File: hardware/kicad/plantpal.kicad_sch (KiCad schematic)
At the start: 58 parts, among them Q1 DMG1012UW, Q2 AO3407, Q3 PMV32UP, Q4 DMG1012UW, Q5 PMV32UP, SW3 RESET, SW4 BOOT, U2 AEM10941-QFN, U3 XC6220, U4 BME688, U5 TPL5110DDCR, U7 ESP32-C6FH4

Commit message: add ext crystal and rtc crystal
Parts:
- added C22, C23: ~, symbol Device:C_Small
- added C3, C4: 12p, symbol Device:C_Small
- added R14, R15: ~, symbol Device:R_Small
- added Y1: CM315D32768DZFT, symbol Device:Crystal_Small
- added Y2: R940000171, symbol Device:Crystal_Small
- renumbered C11 to C1, C17 to C10, C5 to C11, C7 to C12, C8 to C13, C18 to C14, C10 to C15, C19 to C16, C14 to C17, C15 to C18, C12 to C19, C9 to C2, C13 to C20, C6 to C21, C4 to C5, C3 to C6, C2 to C7, C16 to C8, C1 to C9, L2 to L1, L1 to L2, Q2 to Q1, Q3 to Q2, Q4 to Q3, Q1 to Q4, R10 to R1, R15 to R10, R3 to R11, R5 to R12, R4 to R13, R8 to R2, R17 to R3, R18 to R4, R19 to R5, R20 to R6, R6 to R7, R1 to R8, R16 to R9, SW4 to SW1, SW3 to SW2, TP8 to TP2, TP9 to TP3, TP2 to TP4, TP3 to TP5, TP11 to TP6, U7 to U1, U4 to U2, U2 to U3, U3 to U4
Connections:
- net GND: now also C22.1, C23.1, C3.1, C4.1
- net at U1.30 (XTAL_N): now also C22.2, Y2.2
- net at U1.31 (XTAL_P): now also R14.2
- net at U1.6 (GPIO0/XTAL_32K_P/ADC1_CH0): now also R15.1
- net at U1.7 (GPIO1/XTAL_32K_N/ADC1_CH1): now also C4.2, Y1.1
- new net: C23.2, R14.1, Y2.1
- new net: C3.2, R15.2, Y1.2
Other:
- note added: "TODO: Look for other example of 40MHz Crystal"

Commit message: add esp32, usb, charger, power gate, and soil moisture
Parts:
- added AE1: Antenna_Chip, symbol Device:Antenna_Chip
- added C24, C25: DNP, Capacitor_SMD:C_0603_1608Metric_Pad1.08x0.95mm_HandSolder, symbol Device:C_Small
- added C26: 10n, Capacitor_SMD:C_0402_1005Metric, symbol Device:C
- added C27: 100n, Capacitor_SMD:C_0402_1005Metric, symbol Device:C
- added C28: 10u, Capacitor_SMD:C_0603_1608Metric, symbol Device:C_Small
- added C29: 10u, Capacitor_SMD:C_0805_2012Metric, symbol Device:C_Small
- added C30: 1n, Capacitor_SMD:C_0402_1005Metric, symbol Device:C_Small
- added D1: ORANGE, LED_SMD:LED_0603_1608Metric, symbol Device:LED
- added D2: B5819W, Diode_SMD:D_SOD-123, symbol Diode:MBR0540
- added D3: LL4148, Diode_SMD:D_MiniMELF, symbol Diode:LL4148
- added F1: 0.75A, Fuse:Fuse_0805_2012Metric, symbol Device:Polyfuse
- added FB1: MMZ1608B601CTAH0, Inductor_SMD:L_0603_1608Metric, symbol Penguino-STM32WL-LoRa-E5-rescue:Ferrite_Bead-Device
- added J1: U262-161N-4BVC11, bwlr1e_prog:USB_C_Receptacle_XKB_U262-16XN-4BVC11, symbol Connector:USB_C_Receptacle_USB2.0
- added L4: 0, Inductor_SMD:L_0603_1608Metric_Pad1.05x0.95mm_HandSolder, symbol Device:L_Small
- added Q6: MMBT3906, Package_TO_SOT_SMD:SOT-23, symbol Transistor_BJT:MMBT3906
- added R16: 1M, Resistor_SMD:R_0603_1608Metric_Pad0.98x0.95mm_HandSolder, symbol Device:R_Small
- added R17, R18: 5.1K, Resistor_SMD:R_0402_1005Metric, symbol Device:R_Small
- added R19, R24: 10k, Resistor_SMD:R_0402_1005Metric, symbol Device:R_Small_US
- added R20: 10K, Resistor_SMD:R_0402_1005Metric, symbol Device:R_Small
- added R21: 2K, Resistor_SMD:R_0603_1608Metric, symbol Device:R_Small
- added R22: 1M, Resistor_SMD:R_0402_1005Metric, symbol Device:R_Small_US
- added R23: 1K, Resistor_SMD:R_0603_1608Metric, symbol Device:R_Small
- added U6: USBLC6-2P6, Package_TO_SOT_SMD:SOT-666, symbol Power_Protection:USBLC6-2P6
- added U7: MCP73831T-2ACI/OT, Package_TO_SOT_SMD:SOT-23-5, symbol Battery_Management:MCP73831-2-OT
- C5: renamed from C22; value ~ -> 10p
- C6: renamed from C23; value ~ -> 10p
- R15: renamed from R13; value 16.776K -> 16.9K; footprint Resistor_SMD:R_0603_1608Metric -> Resistor_SMD:R_0402_1005Metric
- R3: renamed from R14; value ~ -> 22
- R4: renamed from R15; value ~ -> 22
- Y2: symbol Device:Crystal_Small -> Device:Crystal_GND24_Small
- renumbered C8 to C10, C9 to C11, C10 to C12, C11 to C13, C12 to C14, C13 to C15, C14 to C16, C15 to C17, C16 to C18, C17 to C19, C18 to C20, C19 to C21, C20 to C22, C21 to C23, C5 to C7, C6 to C8, C7 to C9, R8 to R10, R9 to R11, R10 to R12, R11 to R13, R12 to R14, R3 to R5, R4 to R6, R5 to R7, R6 to R8, R7 to R9
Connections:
- net BATT+: now also Q2.2 (S), R7.1
- net DONE: now also R16.1
- net GND: now also Y2.2, Y2.4, AE1.1 (FEED), C24.1, C25.2, C26.2, C27.2, C28.2, C29.1, C30.2, J1.A1 (GND), J1.A12 (GND), J1.B1 (GND), J1.B12 (GND), Q6.3 (C), R16.2, R17.2, R18.2, R21.2, R22.2, U6.2 (GND), U7.2 (VSS)
- net LIPO+: no longer Q2.2 (S), R7.1
- net M_DRV: now also R20.2
- net PWM: now also R19.1, R24.2
- net SENSE_OUT: now also C30.1, D3.1 (K), R22.1
- net at C5.2, U1.30 (XTAL_N): now also Y2.3; no longer Y2.2
- net ANT: now reaches U1.1 (ANT)
- net ANT: now also C25.1, L4.2
- new net: J1.B5 (CC2), R18.1
- new net: C27.1, F1.1, FB1.2
- new net: C26.1, FB1.1, J1.A4 (VBUS), J1.A9 (VBUS), J1.B4 (VBUS), J1.B9 (VBUS)
- new net: J1.A5 (CC1), R17.1
- new net: Q6.1 (B), R24.1
- new net: R23.1, U7.1 (STAT)
- new net: R21.1, U7.5 (PROG)
- new net: AE1.2 (PCB_Trace), C24.2, L4.1
- new net: D1.1 (K), R23.2
- new net: D2.1 (K), R20.1
- new net +BATT: C29.2, U7.3 (VBAT)
- new net CAP_TRACK: D3.2 (A), Q6.2 (E), R19.2
- new net D+: U6.6 (I/O1)
- new net D-: U6.4 (I/O2)
- new net D_IN+: J1.A6 (D+), J1.B6 (D+), U6.1 (I/O1)
- new net D_IN-: J1.A7 (D-), J1.B7 (D-), U6.3 (I/O2)
- new net VBUS: C28.1, D1.2 (A), D2.2 (A), F1.2, U6.5 (VBUS), U7.4 (VDD)
- no-connect marks 7 -> 10
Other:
- note added: "50 ohm Trace Refer to Picoclick-C3 for layout"
- note added: "Around 30s Timer"
- note added: "Battery Charger"
- note added: "Charge LED"
- note added: "Diode might not be needed"
- note added: "NOTE: Pull-down might not be needed for DONE"
- note added: "Place Close to ESP32-C6"
- note added: "Resistor Prog Charge Rate: 10K = 100mA 5K = 200mA 2K = 500mA 1K = 1000mA"
- note added: "Soil Moisture Sense"
- note added: "TODO: - Schematic for EPD"
- note added: "USB-C and ESD Protection"
- note added: "When USB is plugged in pull M_DRV to 3V3"
- note removed: "30s Timer"
- moved on the sheet: C19, C20, C23, C3, C4, C5, C6, R11, R12, R13, R14, R15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

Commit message: separate schematics
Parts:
- removed AE1: Antenna_Chip, symbol Device:Antenna_Chip
- removed BT1: 3.7v LiPo, Connector_JST:JST_PH_S2B-PH-K_1x02_P2.00mm_Horizontal, symbol Device:Battery_Cell
- removed C1: 100n, symbol Device:C_Small
- removed C10: 0.1uF, Capacitor_SMD:C_0603_1608Metric, symbol Device:C
- removed C11, C16, C18, C9: 100n, Capacitor_SMD:C_0603_1608Metric_Pad1.08x0.95mm_HandSolder, symbol Device:C_Small
- removed C12: 10n, Capacitor_SMD:C_0603_1608Metric_Pad1.08x0.95mm_HandSolder, symbol Device:C_Small
- removed C13, C8: 1u, Capacitor_SMD:C_0603_1608Metric_Pad1.08x0.95mm_HandSolder, symbol Device:C_Small
- removed C14: 150u, Capacitor_SMD:C_1210_3225Metric, symbol Device:C_Small
- removed C15: 22u, Capacitor_SMD:C_0603_1608Metric_Pad1.08x0.95mm_HandSolder, symbol Device:C_Small
- removed C17, C21, C22, C7: 10u, Capacitor_SMD:C_0603_1608Metric_Pad1.08x0.95mm_HandSolder, symbol Device:C_Small
- removed C19, C20: 100nF, Capacitor_SMD:C_0603_1608Metric_Pad1.08x0.95mm_HandSolder, symbol Device:C_Small
- removed C2: 1u, symbol Device:C_Small
- removed C23: 100nF, Capacitor_SMD:C_0603_1608Metric, symbol Device:C_Small
- removed C24, C25: DNP, Capacitor_SMD:C_0603_1608Metric_Pad1.08x0.95mm_HandSolder, symbol Device:C_Small
- removed C26: 10n, Capacitor_SMD:C_0402_1005Metric, symbol Device:C
- removed C27: 100n, Capacitor_SMD:C_0402_1005Metric, symbol Device:C
- removed C28: 10u, Capacitor_SMD:C_0603_1608Metric, symbol Device:C_Small
- removed C29: 10u, Capacitor_SMD:C_0805_2012Metric, symbol Device:C_Small
- removed C3, C4: 12p, symbol Device:C_Small
- removed C30: 1n, Capacitor_SMD:C_0402_1005Metric, symbol Device:C_Small
- removed C5, C6: 10p, symbol Device:C_Small
- removed D1: ORANGE, LED_SMD:LED_0603_1608Metric, symbol Device:LED
- removed D2: B5819W, Diode_SMD:D_SOD-123, symbol Diode:MBR0540
- removed D3: LL4148, Diode_SMD:D_MiniMELF, symbol Diode:LL4148
- removed F1: 0.75A, Fuse:Fuse_0805_2012Metric, symbol Device:Polyfuse
- removed FB1: MMZ1608B601CTAH0, Inductor_SMD:L_0603_1608Metric, symbol Penguino-STM32WL-LoRa-E5-rescue:Ferrite_Bead-Device
- removed J1: U262-161N-4BVC11, bwlr1e_prog:USB_C_Receptacle_XKB_U262-16XN-4BVC11, symbol Connector:USB_C_Receptacle_USB2.0
- removed L1: 2n, Inductor_SMD:L_0603_1608Metric_Pad1.05x0.95mm_HandSolder, symbol Device:L_Small
- removed L2: 10u 0.55A, Teapot:IND_LPS4012-103MRB, symbol Device:L_Small
- removed L3: 10u, Inductor_SMD:L_0603_1608Metric_Pad1.05x0.95mm_HandSolder, symbol Device:L_Small
- removed L4: 0, Inductor_SMD:L_0603_1608Metric_Pad1.05x0.95mm_HandSolder, symbol Device:L_Small
- removed Q1: AO3407, Package_TO_SOT_SMD:SOT-23, symbol Device:Q_PMOS_GSD
- removed Q2: PMV32UP, Package_TO_SOT_SMD:SOT-23, symbol Device:Q_PMOS_GSD
- removed Q3, Q4: DMG1012UW, Package_TO_SOT_SMD:SOT-323_SC-70, symbol Device:Q_NMOS_GSD
- removed Q5: PMV32UP, Package_TO_SOT_SMD:SOT-23, symbol Simulation_SPICE:PMOS
- removed Q6: MMBT3906, Package_TO_SOT_SMD:SOT-23, symbol Transistor_BJT:MMBT3906
- removed R1: 5.1K, symbol Device:R_Small
- removed R10, R16: 1M, Resistor_SMD:R_0603_1608Metric_Pad0.98x0.95mm_HandSolder, symbol Device:R_Small
- removed R11, R12: 10K, Resistor_SMD:R_0603_1608Metric_Pad0.98x0.95mm_HandSolder, symbol Device:R_Small
- removed R13, R14, R6: 10K, Resistor_SMD:R_0603_1608Metric, symbol Device:R_Small
- removed R15: 16.9K, Resistor_SMD:R_0402_1005Metric, symbol Device:R_Small
- removed R17, R18: 5.1K, Resistor_SMD:R_0402_1005Metric, symbol Device:R_Small
- removed R19, R24: 10k, Resistor_SMD:R_0402_1005Metric, symbol Device:R_Small_US
- removed R2, R9: 10K, symbol Device:R_Small
- removed R20: 10K, Resistor_SMD:R_0402_1005Metric, symbol Device:R_Small
- removed R21: 2K, Resistor_SMD:R_0603_1608Metric, symbol Device:R_Small
- removed R22: 1M, Resistor_SMD:R_0402_1005Metric, symbol Device:R_Small_US
- removed R23: 1K, Resistor_SMD:R_0603_1608Metric, symbol Device:R_Small
- removed R3, R4: 22, symbol Device:R_Small
- removed R5: 4.7K, Resistor_SMD:R_0603_1608Metric, symbol Device:R_Small
- removed R7, R8: 1M, Resistor_SMD:R_0603_1608Metric, symbol Device:R_Small
- removed SC1, SC2, SC3, SC4: KXOB25-05X3F, Teapot:KXOB25-05X3F, symbol Device:Solar_Cell
- removed SW1: BOOT, symbol Switch:SW_Push
- removed SW2: RESET, symbol Switch:SW_Push
- removed TP1: BATT+, TestPoint:TestPoint_Pad_D1.5mm, symbol Connector:TestPoint
- removed TP2: DL_RXD0, symbol Connector:TestPoint
- removed TP3: DL_TXD0, symbol Connector:TestPoint
- removed TP4: SOLAR+, TestPoint:TestPoint_Pad_D1.5mm, symbol Connector:TestPoint
- removed TP5: SOLAR-, TestPoint:TestPoint_Pad_D1.5mm, symbol Connector:TestPoint
- removed TP6: 3V3, TestPoint:TestPoint_Pad_D1.5mm, symbol Connector:TestPoint
- removed U1: ESP32-C6FH4, Package_DFN_QFN:QFN-32-1EP_5x5mm_P0.5mm_EP3.6x3.6mm, symbol Espressif:ESP32-C6FH4
- removed U2: BME688, Teapot:BME680-PSON80P300X300X100-8N, symbol Sensor:BME680
- removed U3: AEM10941-QFN, Package_DFN_QFN:QFN-28-1EP_5x5mm_P0.5mm_EP3.35x3.35mm, symbol Teapot:AEM10941-QFN
- removed U4: XC6220, Package_TO_SOT_SMD:SOT-23-5, symbol Teapot:XC6220
- removed U5: TPL5110DDCR, Teapot:SOT95P280X110-6N, symbol cwlr1a:TPL5110DDCR
- removed U6: USBLC6-2P6, Package_TO_SOT_SMD:SOT-666, symbol Power_Protection:USBLC6-2P6
- removed U7: MCP73831T-2ACI/OT, Package_TO_SOT_SMD:SOT-23-5, symbol Battery_Management:MCP73831-2-OT
- removed Y1: CM315D32768DZFT, symbol Device:Crystal_Small
- removed Y2: R940000171, symbol Device:Crystal_GND24_Small
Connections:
- no-connect marks 10 -> 0
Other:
- added sheet Battery (battery.kicad_sch)
- added sheet Display (display.kicad_sch)
- added sheet Main Controller (main_controller.kicad_sch)
- added sheet Power Switch and Regulator (power_switch_and_regulator.kicad_sch)
- added sheet Sensor (sensor.kicad_sch)
- added sheet Solar Power (solar_power.kicad_sch)
- added sheet USB Power (usb_power.kicad_sch)
- note removed: "3.3V Regulator (Max 1000mA)"
- note removed: "3.7v LiPo Battery Input and Polar Protection"
- note removed: "50 ohm Trace Refer to Picoclick-C3 for layout"
- note removed: "6-Pin to control EPD"
- note removed: "Around 30s Timer"
- note removed: "BME680 Environmental Sensor over I2C"
- note removed: "Battery Charger"
- note removed: "Battery Measurement"
- note removed: "Charge LED"
- note removed: "Diode might not be needed"
- note removed: "Download Pins"
- note removed: "NOTE: Pull-down might not be needed for DONE"
- note removed: "PWM and SENSE_OUT are for Soil Moisture Sensing"
- note removed: "Place Close to ESP32-C6"
- note removed: "RC Delay Circuit & Reset Button"
- note removed: "Read on first 3ms after boot"
- note removed: "Resistor Prog Charge Rate: 10K = 100mA 5K = 200mA 2K = 500mA 1K = 1000mA"
- note removed: "See ESP32-C6 Hardware Design Guidelines Chapter 2.2"
- note removed: "Soil Moisture Sense"
- note removed: "Solar Cell Input"
- note removed: "Solar Charger"
- note removed: "Strapping Pin are shared with Power Status"
- note removed: "TODO: - Schematic for EPD"
- note removed: "TODO: Look for other example of 40MHz Crystal"
- note removed: "Toggle Low to High for valid Done Signal"
- note removed: "USB-C and ESD Protection"
- note removed: "When USB is plugged in pull M_DRV to 3V3"

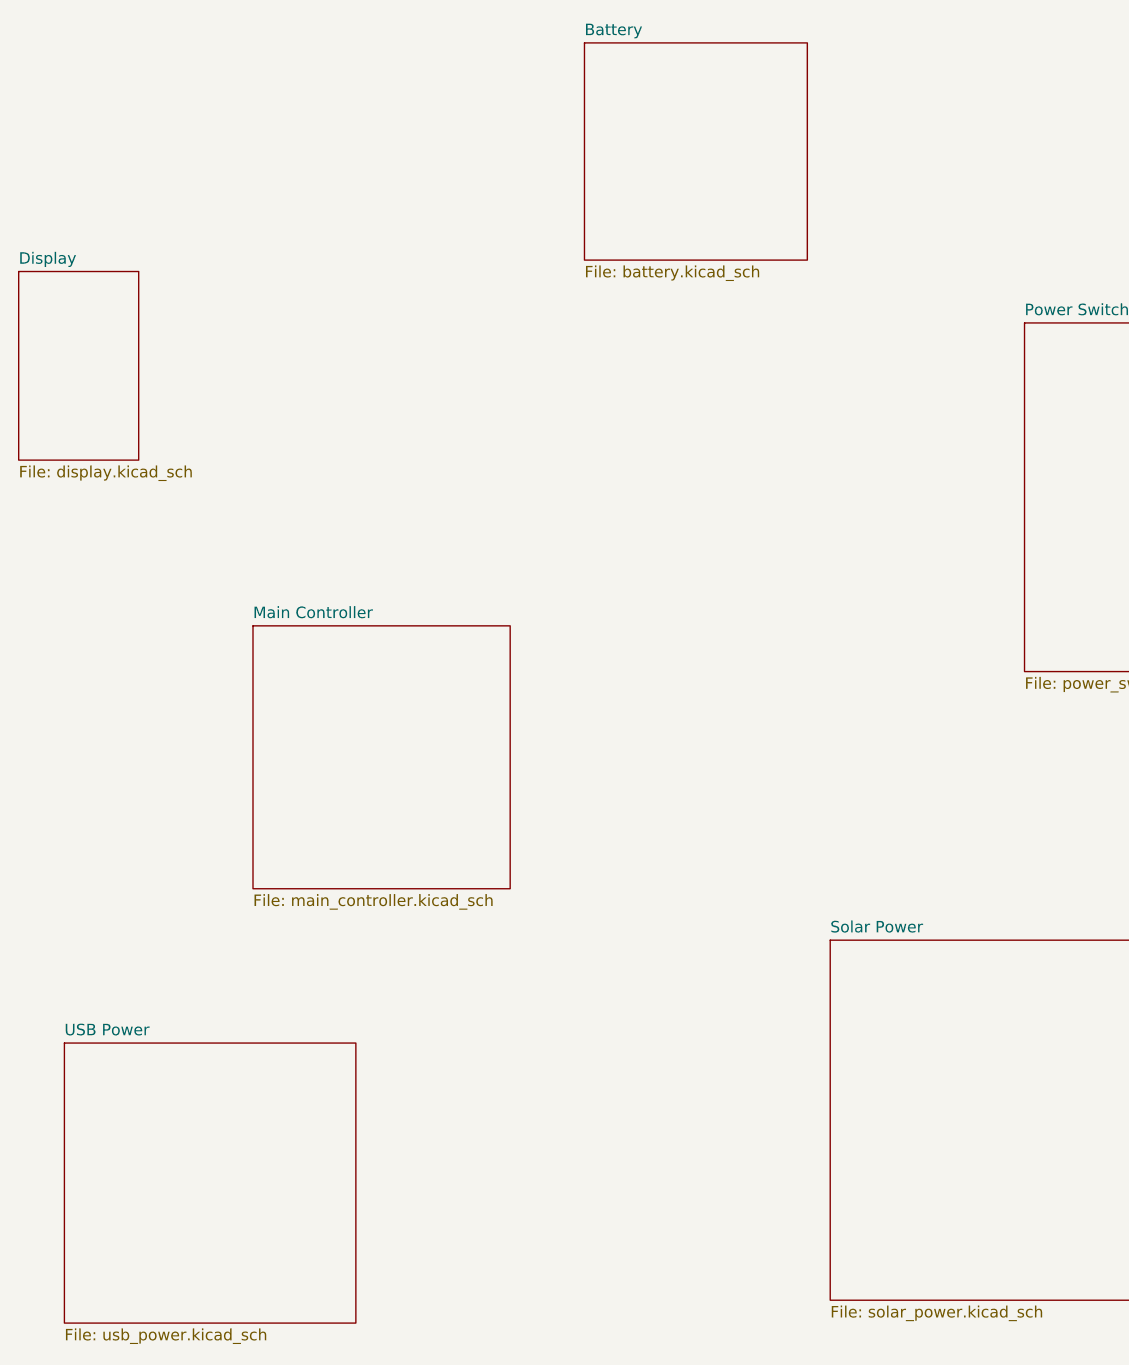
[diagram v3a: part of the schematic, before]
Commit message: fix label
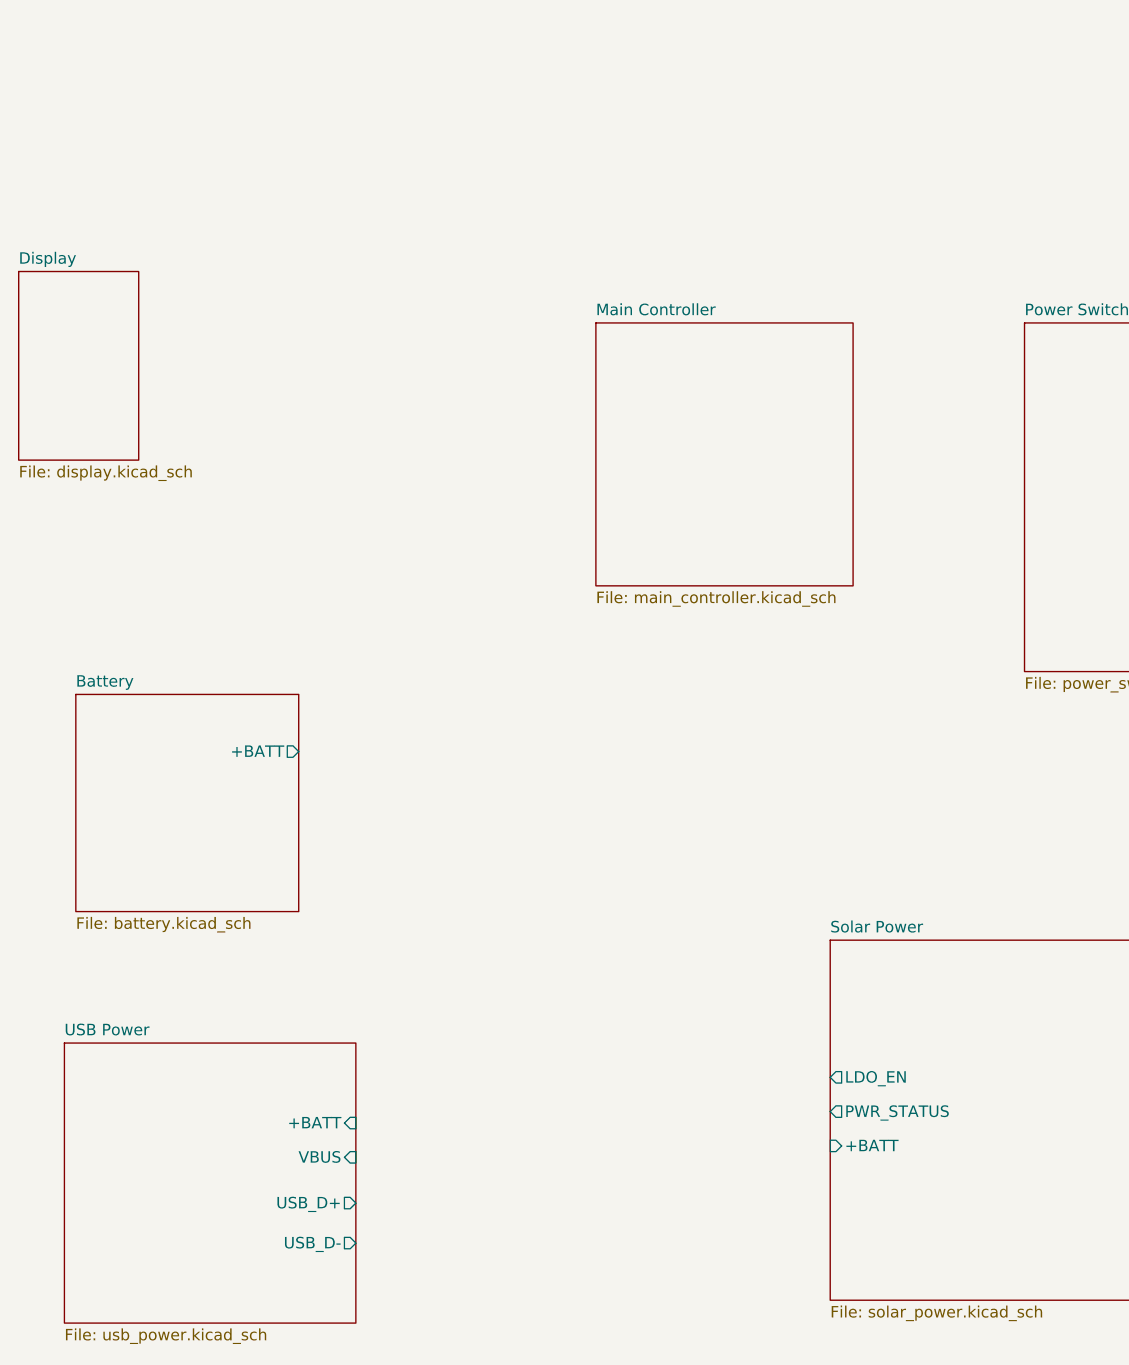
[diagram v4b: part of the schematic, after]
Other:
- sheet Battery ports: added +BATT; removed none
- sheet Solar Power ports: added +BATT, LDO_EN, PWR_STATUS; removed none
- sheet USB Power ports: added +BATT, USB_D+, USB_D-, VBUS; removed none
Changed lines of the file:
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@@
     )
   )
-  (sheet (at 107.95 40.005) (size 24.765 24.13) (fields_autoplaced)
+  (sheet (at 51.435 112.395) (size 24.765 24.13) (fields_autoplaced)
     (stroke (width 0.1524) (type solid))
     (fill (color 0 0 0 0.0000))
-    (property "Sheetname" "Battery" (at 107.95 39.2934 0)
+    (property "Sheetname" "Battery" (at 51.435 111.6834 0)
       (effects (font (size 1.27 1.27)) (justify left bottom))
     )
-    (property "Sheetfile" "battery.kicad_sch" (at 107.95 64.7196 0)
+    (property "Sheetfile" "battery.kicad_sch" (at 51.435 137.1096 0)
       (effects (font (size 1.27 1.27)) (justify left top))
+    )
+    (pin "+BATT" output (at 76.2 118.745 0)
+      (effects (font (size 1.27 1.27)) (justify right))
     )
     (instances
@@
       (effects (font (size 1.27 1.27)) (justify left top))
     )
+    (pin "+BATT" input (at 82.55 160.02 0)
+      (effects (font (size 1.27 1.27)) (justify right))
+    )
+    (pin "VBUS" input (at 82.55 163.83 0)
+      (effects (font (size 1.27 1.27)) (justify right))
+    )
+    (pin "USB_D+" output (at 82.55 168.91 0)
+      (effects (font (size 1.27 1.27)) (justify right))
+    )
+    (pin "USB_D-" output (at 82.55 173.355 0)
+      (effects (font (size 1.27 1.27)) (justify right))
+    )
     (instances
       (project "plantpal"
@@
       (effects (font (size 1.27 1.27)) (justify left top))
     )
+    (pin "LDO_EN" output (at 135.255 154.94 180)
+      (effects (font (size 1.27 1.27)) (justify left))
+    )
+    (pin "PWR_STATUS" output (at 135.255 158.75 180)
+      (effects (font (size 1.27 1.27)) (justify left))
+    )
+    (pin "+BATT" input (at 135.255 162.56 180)
+      (effects (font (size 1.27 1.27)) (justify left))
+    )
     (instances
       (project "plantpal"
@@
     )
   )
-  (sheet (at 71.12 104.775) (size 28.575 29.21) (fields_autoplaced)
+  (sheet (at 109.22 71.12) (size 28.575 29.21) (fields_autoplaced)
     (stroke (width 0.1524) (type solid))
     (fill (color 0 0 0 0.0000))
-    (property "Sheetname" "Main Controller" (at 71.12 104.0634 0)
+    (property "Sheetname" "Main Controller" (at 109.22 70.4084 0)
       (effects (font (size 1.27 1.27)) (justify left bottom))
     )
-    (property "Sheetfile" "main_controller.kicad_sch" (at 71.12 134.5696 0)
+    (property "Sheetfile" "main_controller.kicad_sch" (at 109.22 100.9146 0)
       (effects (font (size 1.27 1.27)) (justify left top))
     )

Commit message: schematic restructure update
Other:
- sheet Main Controller ports: added +3V3, BATT_MEAS, BATT_MEAS_EN, DONE, M_DRV, PWM, PWR_STATUS, SCL, SDA, SENSE_OUT, USB_D+, USB_D-; removed none
- sheet Power Switch and Regulator ports: added +3V3, +BATT, DONE, LDO_EN, M_DRV, VBUS; removed none
- sheet Sensor ports: added +3V3, +BATT, BATT_MEAS, BATT_MEAS_EN, PWM, SCL, SDA, SENSE_OUT; removed none

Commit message: beautify schematic
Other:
- sheet Power Switch and Regulator renamed Power Gate and Regulator
- sheet Power Gate and Regulator: file power_switch_and_regulator.kicad_sch -> power_gate_and_regulator.kicad_sch
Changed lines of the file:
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@@
     (stroke (width 0.1524) (type solid))
     (fill (color 0 0 0 0.0000))
-    (property "Sheetname" "Power Switch and Regulator" (at 105.41 107.2384 0)
+    (property "Sheetname" "Power Gate and Regulator" (at 105.41 107.2384 0)
       (effects (font (size 1.27 1.27)) (justify left bottom))
     )
-    (property "Sheetfile" "power_switch_and_regulator.kicad_sch" (at 105.41 123.7746 0)
+    (property "Sheetfile" "power_gate_and_regulator.kicad_sch" (at 105.41 123.7746 0)
       (effects (font (size 1.27 1.27)) (justify left top))
     )
